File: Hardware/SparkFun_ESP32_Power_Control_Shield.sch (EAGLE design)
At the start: 67 parts, among them IC1 LMV358, IC2 LMV358, J2 POWER_JACKPTH_LOCK, U1 MC33926, U2 MC33926, U3 MC33926, U4 R-78E5.0-1.0

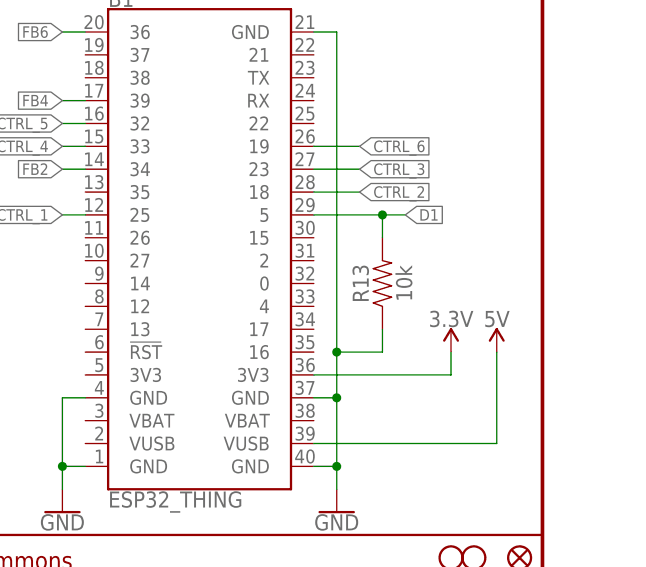
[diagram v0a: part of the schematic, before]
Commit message: Replaced R13
Pull down resistor R13 was too weak for the ESP32 at 10k. Replacing with
1k.
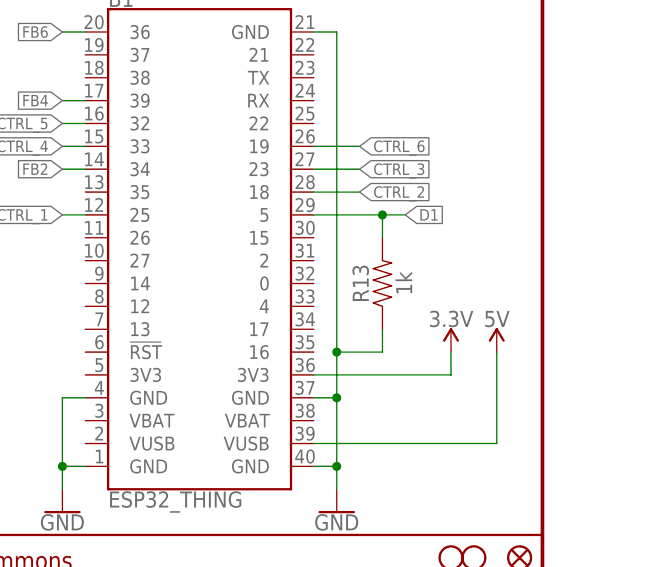
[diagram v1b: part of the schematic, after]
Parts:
- R13: value 10k -> 1k; device SparkFun-Resistors:10KOHM-0603-1/10W-1% -> SparkFun-Resistors:1KOHM-0603-1/10W-1%
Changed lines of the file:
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@@
 <part name="GND18" library="SparkFun-PowerSymbols" deviceset="GND" device=""/>
 <part name="SUPPLY16" library="SparkFun-PowerSymbols" deviceset="5V" device=""/>
-<part name="R13" library="SparkFun-Resistors" deviceset="10KOHM" device="-0603-1/10W-1%" value="10k"/>
+<part name="R13" library="SparkFun-Resistors" deviceset="1KOHM" device="-0603-1/10W-1%" value="1k"/>
 <part name="R10" library="SparkFun-Resistors" deviceset="1KOHM" device="-HORIZ-1/4W-1%" value=""/>
 <part name="JP2" library="SparkFun-Jumpers" deviceset="JUMPER-SMT_2_NC_PASTE" device="_NO-SILK" value=""/>
